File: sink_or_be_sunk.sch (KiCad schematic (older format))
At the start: 0 parts

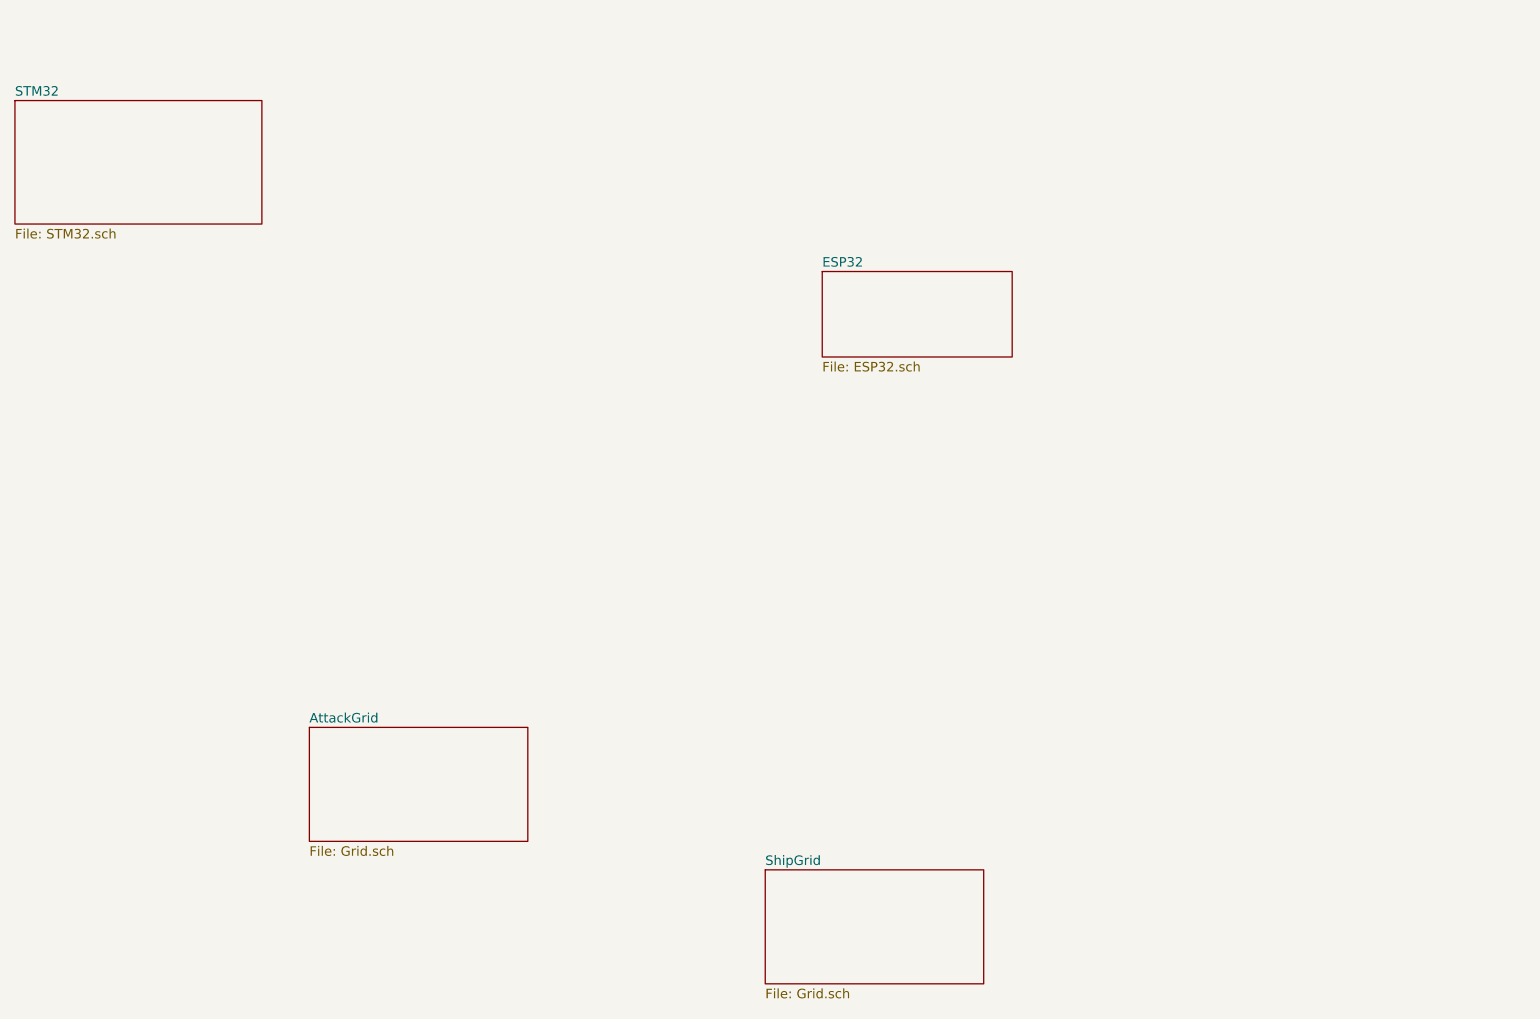
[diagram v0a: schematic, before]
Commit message: updated the readme and added example of heirarchical labels
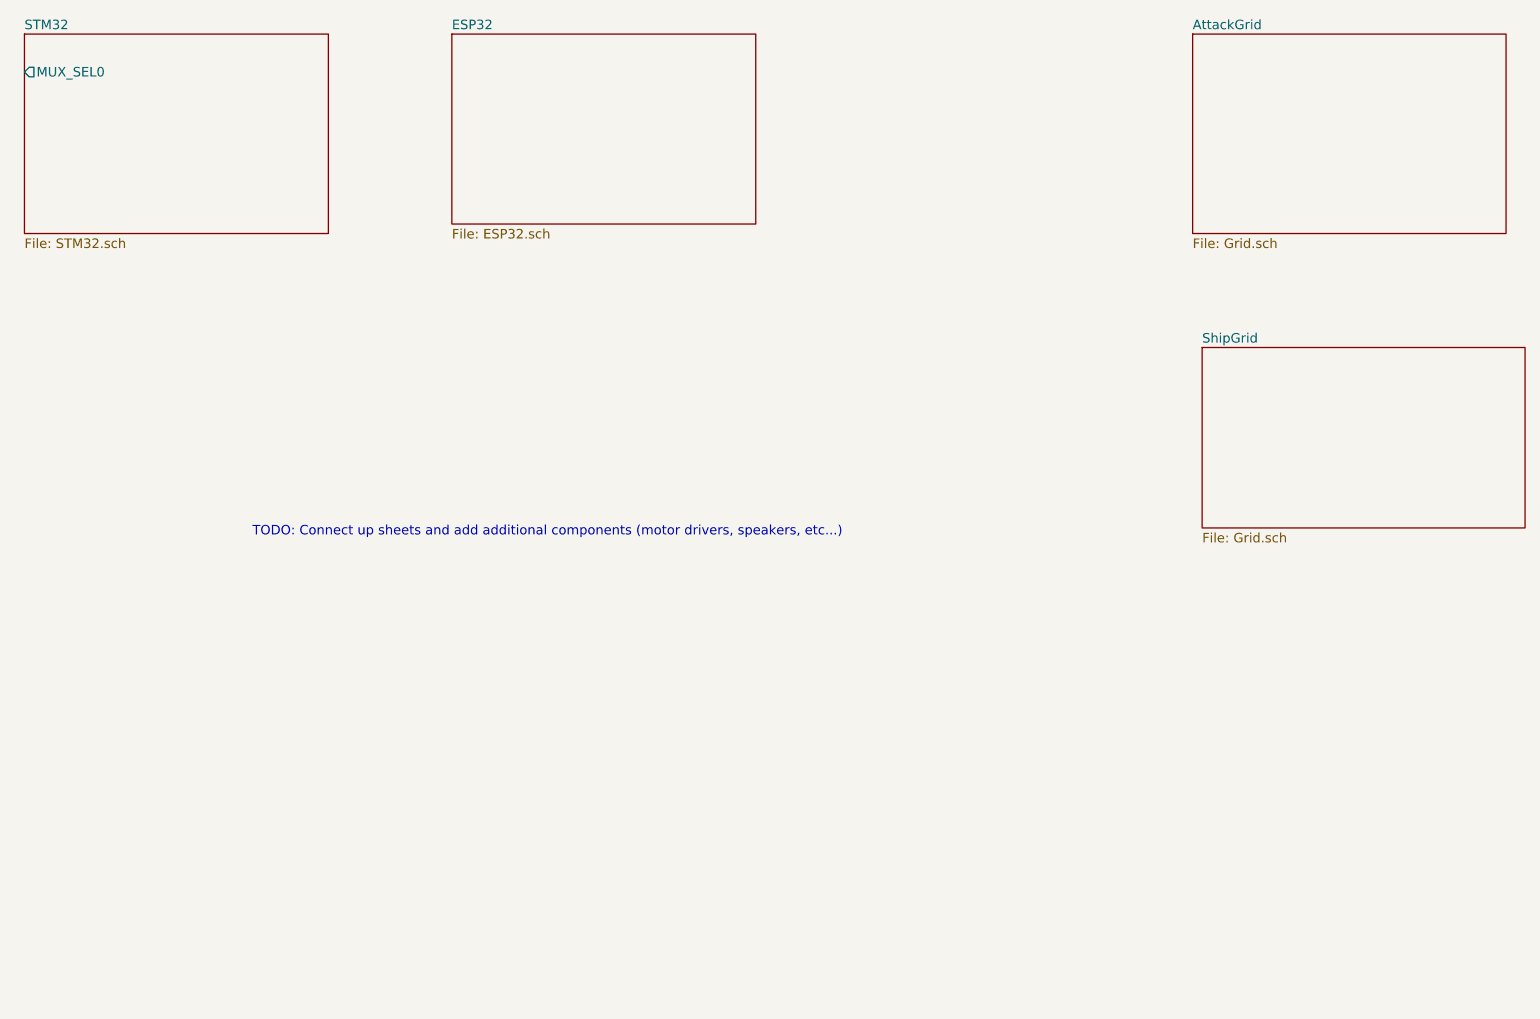
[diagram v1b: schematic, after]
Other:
- note added: "TODO: Connect up sheets and add additional components (motor drivers, speakers, etc...)"
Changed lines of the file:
@@
 $EndDescr
 $Sheet
-S 1450 1700 1300 650
+S 1500 1350 1600 1050
 U 613246BD
 F0 "STM32" 50
 F1 "STM32.sch" 50
+F2 "MUX_SEL0" O L 1500 1550 50
 $EndSheet
 $Sheet
-S 5700 2600 1000 450
+S 3750 1350 1600 1000
 U 613B739E
 F0 "ESP32" 50
@@
 $EndSheet
 $Sheet
-S 3000 5000 1150 600
+S 7650 1350 1650 1050
 U 613B79B3
 F0 "AttackGrid" 50
@@
 $EndSheet
 $Sheet
-S 5400 5750 1150 600
+S 7700 3000 1700 950
 U 613B7770
 F0 "ShipGrid" 50
 F1 "Grid.sch" 50
 $EndSheet
+Text Notes 2700 4000 0    50   ~ 0
+TODO: Connect up sheets and add additional components (motor drivers, speakers, etc...)
 $EndSCHEMATC

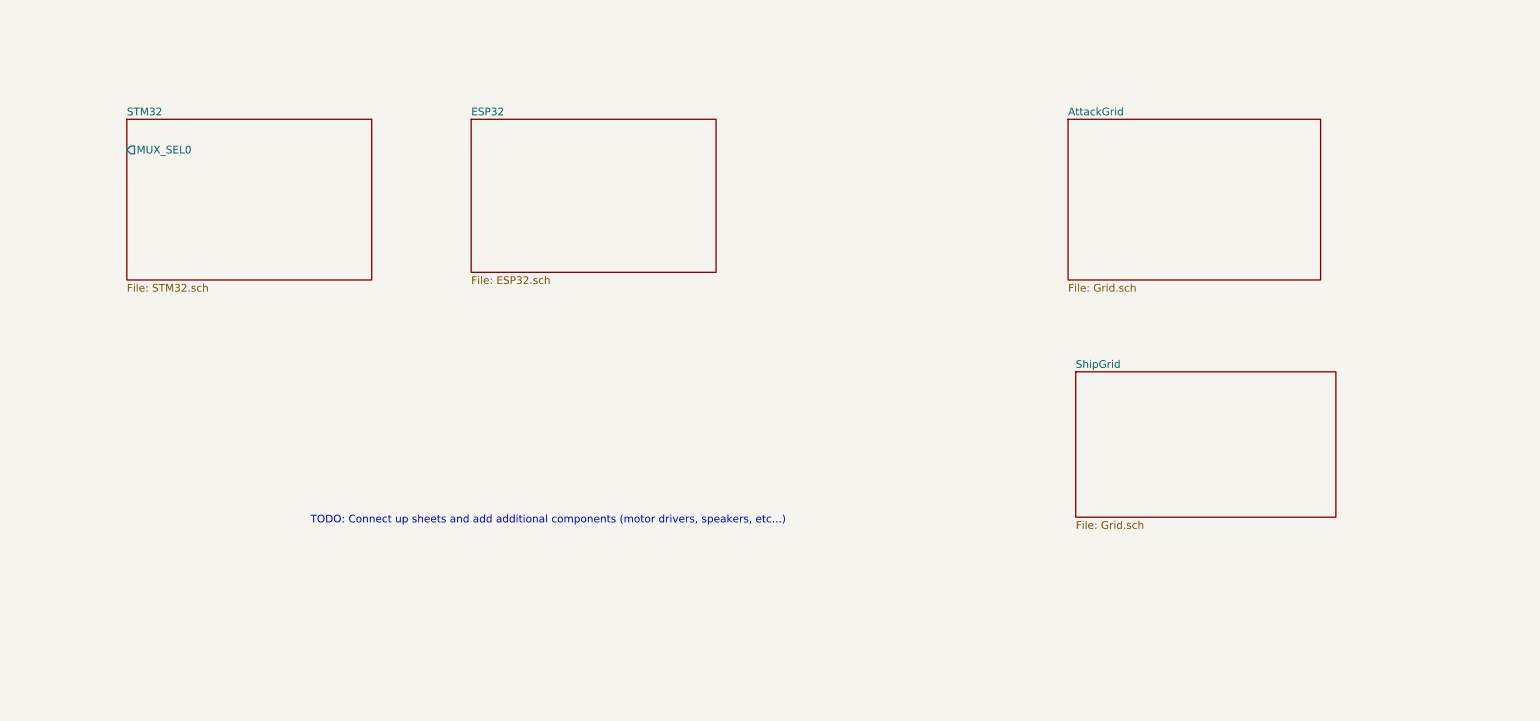
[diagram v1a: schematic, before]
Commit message: removed unneeded sheets and added speaker sheet/circuit
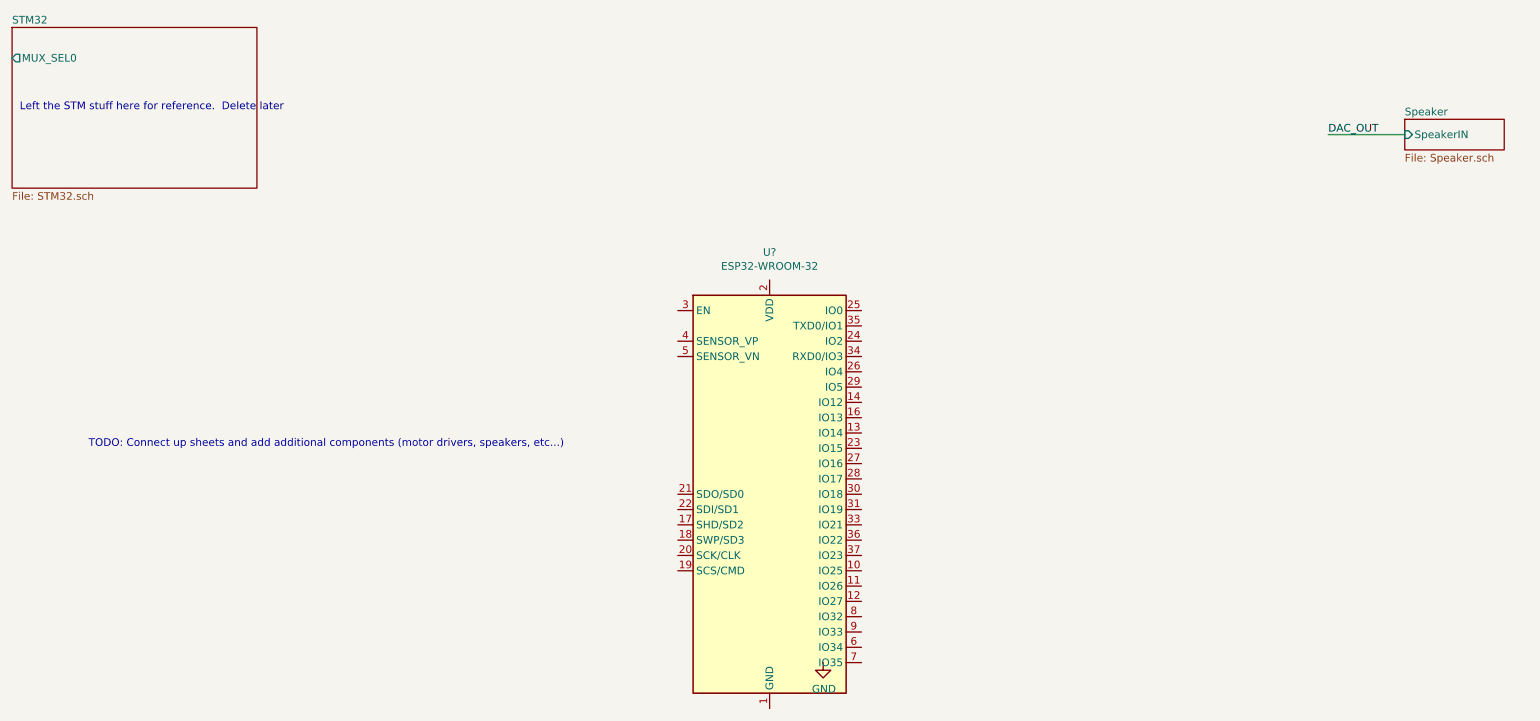
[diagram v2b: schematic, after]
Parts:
- added U?: ESP32-WROOM-32, RF_Module:ESP32-WROOM-32, symbol RF_Module:ESP32-WROOM-32
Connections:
- new net: U?.1 (GND), U?.15 (GND), U?.38 (GND), U?.39 (GND)
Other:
- note added: "Left the STM stuff here for reference. Delete later"
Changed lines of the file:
@@
 $Descr A4 11693 8268
 encoding utf-8
-Sheet 1 5
+Sheet 1 3
 Title "Main Layout"
 Date "2021-09-01"
@@
 $EndDescr
 $Sheet
-S 1500 1350 1600 1050
+S 750  750  1600 1050
 U 613246BD
 F0 "STM32" 50
 F1 "STM32.sch" 50
-F2 "MUX_SEL0" O L 1500 1550 50
+F2 "MUX_SEL0" O L 750 950 50
 $EndSheet
+Text Notes 1250 3500 0    50   ~ 0
+TODO: Connect up sheets and add additional components (motor drivers, speakers, etc...)
 $Sheet
-S 3750 1350 1600 1000
-U 613B739E
-F0 "ESP32" 50
-F1 "ESP32.sch" 50
+S 9850 1350 650  200
+U 6144DCFC
+F0 "Speaker" 50
+F1 "Speaker.sch" 50
+F2 "SpeakerIN" I L 9850 1450 50
 $EndSheet
-$Sheet
-S 7650 1350 1650 1050
-U 613B79B3
-F0 "AttackGrid" 50
-F1 "Grid.sch" 50
-$EndSheet
-$Sheet
-S 7700 3000 1700 950
-U 613B7770
-F0 "ShipGrid" 50
-F1 "Grid.sch" 50
-$EndSheet
-Text Notes 2700 4000 0    50   ~ 0
-TODO: Connect up sheets and add additional components (motor drivers, speakers, etc...)
+Text Notes 800  1300 0    50   ~ 0
+Left the STM stuff here for reference.  Delete later
+$Comp
+L RF_Module:ESP32-WROOM-32 U?
+U 1 1 6147878D
+P 5700 3800
+AR Path="/613B739E/6147878D" Ref="U?"  Part="1"
+AR Path="/6147878D" Ref="U?"  Part="1"
+F 0 "U?" H 5700 5381 50  0000 C CNN
+F 1 "ESP32-WROOM-32" H 5700 5290 50  0000 C CNN
+F 2 "RF_Module:ESP32-WROOM-32" H 5700 2300 50  0001 C CNN
+F 3 "https://www.espressif.com/sites/default/files/documentation/esp32-wroom-32_datasheet_en.pdf" H 5400 3850 50  0001 C CNN
+	1    5700 3800
+	1    0    0    -1
+$EndComp
+$Comp
+L power:GND #PWR?
+U 1 1 61478793
+P 6050 4900
+F 0 "#PWR?" H 6050 4650 50  0001 C CNN
+F 1 "GND" H 6055 4727 50  0000 C CNN
+F 2 "" H 6050 4900 50  0001 C CNN
+F 3 "" H 6050 4900 50  0001 C CNN
+	1    6050 4900
+	1    0    0    -1
+$EndComp
+Wire Wire Line
+	9850 1450 9350 1450
+Text Label 9350 1450 0    50   ~ 0
+DAC_OUT
 $EndSCHEMATC

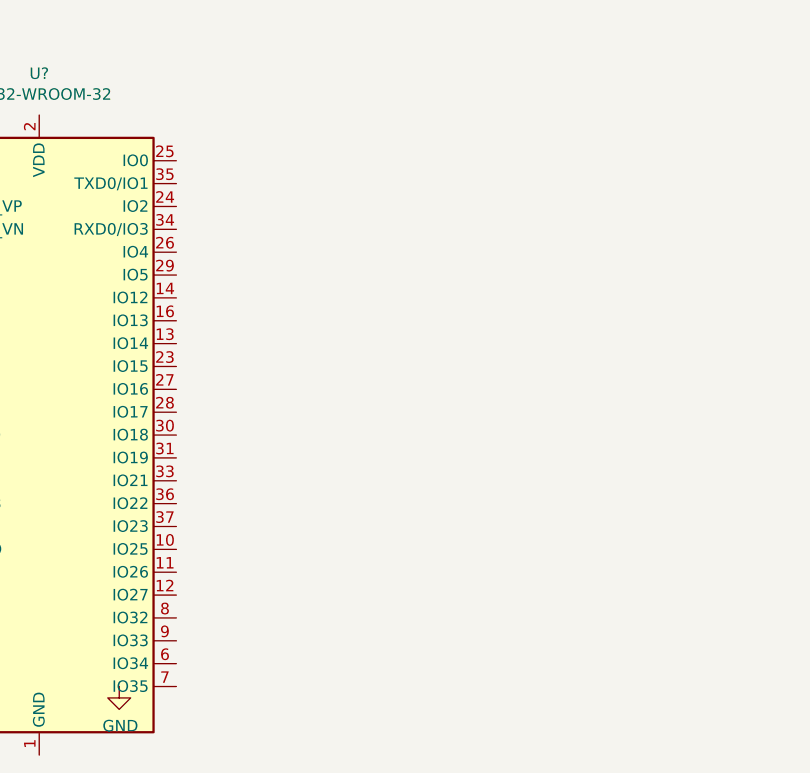
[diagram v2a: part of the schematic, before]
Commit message: added all pin definitions
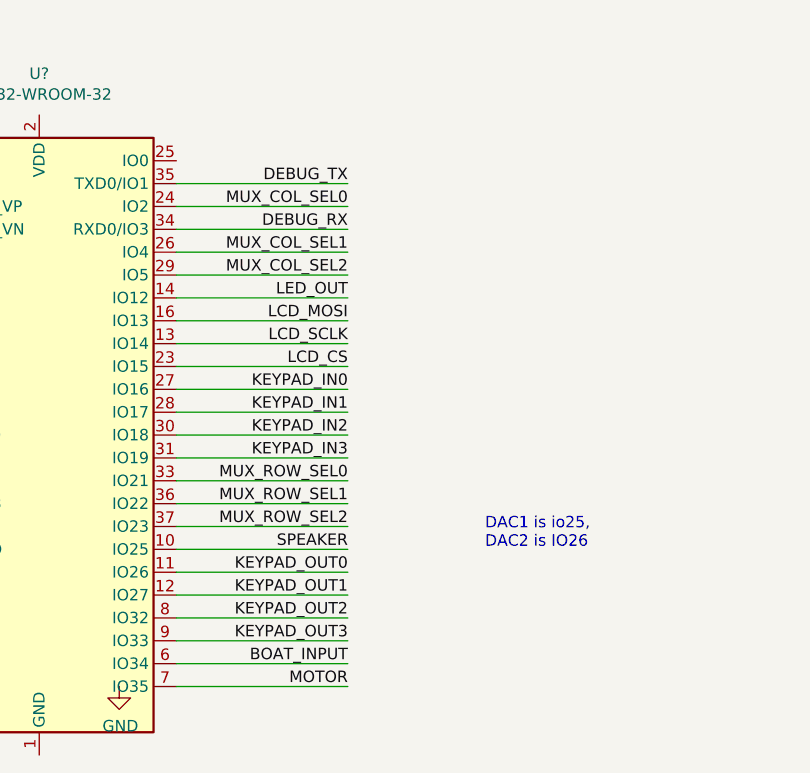
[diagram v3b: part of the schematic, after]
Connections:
- net SPEAKER: now reaches U?.10 (IO25)
- net KEYPAD_OUT0: now reaches U?.11 (IO26)
- net KEYPAD_OUT1: now reaches U?.12 (IO27)
- net LCD_SCLK: now reaches U?.13 (IO14)
- net LED_OUT: now reaches U?.14 (IO12)
- net LCD_MOSI: now reaches U?.16 (IO13)
- net LCD_CS: now reaches U?.23 (IO15)
- net MUX_COL_SEL0: now reaches U?.24 (IO2)
- net MUX_COL_SEL1: now reaches U?.26 (IO4)
- net KEYPAD_IN0: now reaches U?.27 (IO16)
- net KEYPAD_IN1: now reaches U?.28 (IO17)
- net MUX_COL_SEL2: now reaches U?.29 (IO5)
- net KEYPAD_IN2: now reaches U?.30 (IO18)
- net KEYPAD_IN3: now reaches U?.31 (IO19)
- net MUX_ROW_SEL0: now reaches U?.33 (IO21)
- net DEBUG_RX: now reaches U?.34 (RXD0/IO3)
- net DEBUG_TX: now reaches U?.35 (TXD0/IO1)
- net MUX_ROW_SEL1: now reaches U?.36 (IO22)
- net MUX_ROW_SEL2: now reaches U?.37 (IO23)
- net BOAT_INPUT: now reaches U?.6 (IO34)
- net MOTOR: now reaches U?.7 (IO35)
- net KEYPAD_OUT2: now reaches U?.8 (IO32)
- net KEYPAD_OUT3: now reaches U?.9 (IO33)
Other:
- note added: "DAC1 is io25,\nDAC2 is IO26"
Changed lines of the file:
@@
 Text Label 9350 1450 0    50   ~ 0
 DAC_OUT
+Wire Wire Line
+	6300 4000 7050 4000
+Text Label 7050 4000 2    50   ~ 0
+MUX_ROW_SEL0
+Wire Wire Line
+	6300 4100 7050 4100
+Text Label 7050 4100 2    50   ~ 0
+MUX_ROW_SEL1
+Wire Wire Line
+	6300 4200 7050 4200
+Text Label 7050 4200 2    50   ~ 0
+MUX_ROW_SEL2
+Wire Wire Line
+	6300 3300 7050 3300
+Text Label 7050 3300 2    50   ~ 0
+LCD_MOSI
+Wire Wire Line
+	6300 3400 7050 3400
+Text Label 7050 3400 2    50   ~ 0
+LCD_SCLK
+Wire Wire Line
+	6300 3500 7050 3500
+Text Label 7050 3500 2    50   ~ 0
+LCD_CS
+Wire Wire Line
+	6300 4300 7050 4300
+Text Label 7050 4300 2    50   ~ 0
+SPEAKER
+Wire Wire Line
+	6300 3600 7050 3600
+Text Label 7050 3600 2    50   ~ 0
+KEYPAD_IN0
+Wire Wire Line
+	6300 3700 7050 3700
+Text Label 7050 3700 2    50   ~ 0
+KEYPAD_IN1
+Wire Wire Line
+	6300 3800 7050 3800
+Text Label 7050 3800 2    50   ~ 0
+KEYPAD_IN2
+Wire Wire Line
+	6300 3900 7050 3900
+Text Label 7050 3900 2    50   ~ 0
+KEYPAD_IN3
+Wire Wire Line
+	6300 4400 7050 4400
+Text Label 7050 4400 2    50   ~ 0
+KEYPAD_OUT0
+Wire Wire Line
+	6300 4500 7050 4500
+Text Label 7050 4500 2    50   ~ 0
+KEYPAD_OUT1
+Wire Wire Line
+	6300 4600 7050 4600
+Text Label 7050 4600 2    50   ~ 0
+KEYPAD_OUT2
+Wire Wire Line
+	6300 4700 7050 4700
+Text Label 7050 4700 2    50   ~ 0
+KEYPAD_OUT3
+Wire Wire Line
+	6300 3200 7050 3200
+Text Label 7050 3200 2    50   ~ 0
+LED_OUT
+Wire Wire Line
+	6300 2800 7050 2800
+Text Label 7050 2800 2    50   ~ 0
+MUX_COL_SEL0
+Wire Wire Line
+	6300 3000 7050 3000
+Text Label 7050 3000 2    50   ~ 0
+MUX_COL_SEL1
+Text Label 7050 3100 2    50   ~ 0
+MUX_COL_SEL2
+Wire Wire Line
+	7050 3100 6300 3100
+Wire Wire Line
+	6300 2900 7050 2900
+Text Label 7050 2900 2    50   ~ 0
+DEBUG_RX
+Wire Wire Line
+	6300 2700 7050 2700
+Text Label 7050 2700 2    50   ~ 0
+DEBUG_TX
+Wire Wire Line
+	6300 4800 7050 4800
+Text Label 7050 4800 2    50   ~ 0
+BOAT_INPUT
+Text Notes 7650 4300 0    50   ~ 0
+DAC1 is io25,\nDAC2 is IO26
+Wire Wire Line
+	6300 4900 7050 4900
+Text Label 7050 4900 2    50   ~ 0
+MOTOR
 $EndSCHEMATC
